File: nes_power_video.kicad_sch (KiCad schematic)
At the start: 13 parts, among them J2 Audio, J3 Video, J4 Conn_01x05, Q1 2SA1015

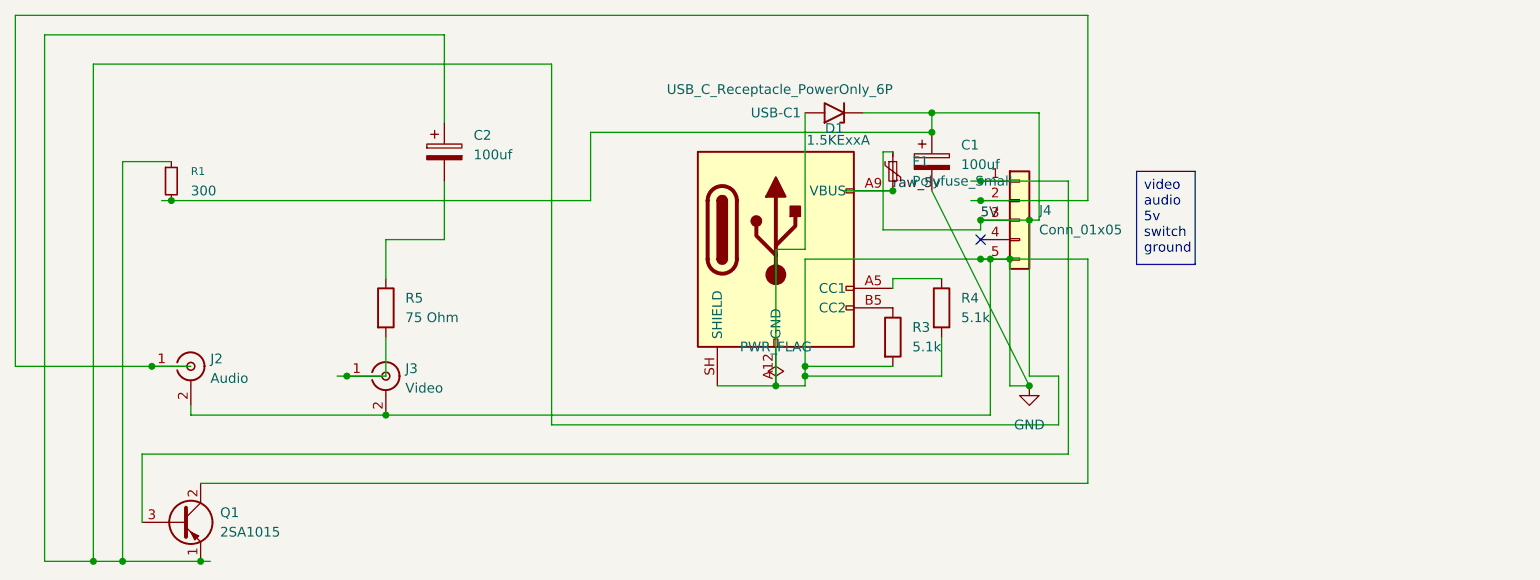
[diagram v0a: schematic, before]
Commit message: Switch J2/J3 to real PJRAN1X1U03X RCA jack symbols and re-route
J2 (Audio) and J3 (Video) were still using the generic
Connector:Conn_Coaxial symbol with the nes1:"nes connector" footprint.
Both now use the dedicated PJRAN1X1U03X symbol and matching footprint,
so the schematic and the board agree with the parts actually fitted.

PCB re-routed around the updated jacks: 47 -> 70 track segments, 6 -> 4
vias, footprint set unchanged.

Also stop tracking KiCad transient files (_autosave-*, *.lck) that were
committed by mistake, and add them to .gitignore.

Co-Authored-By: Claude Opus 5 <noreply@anthropic.com>
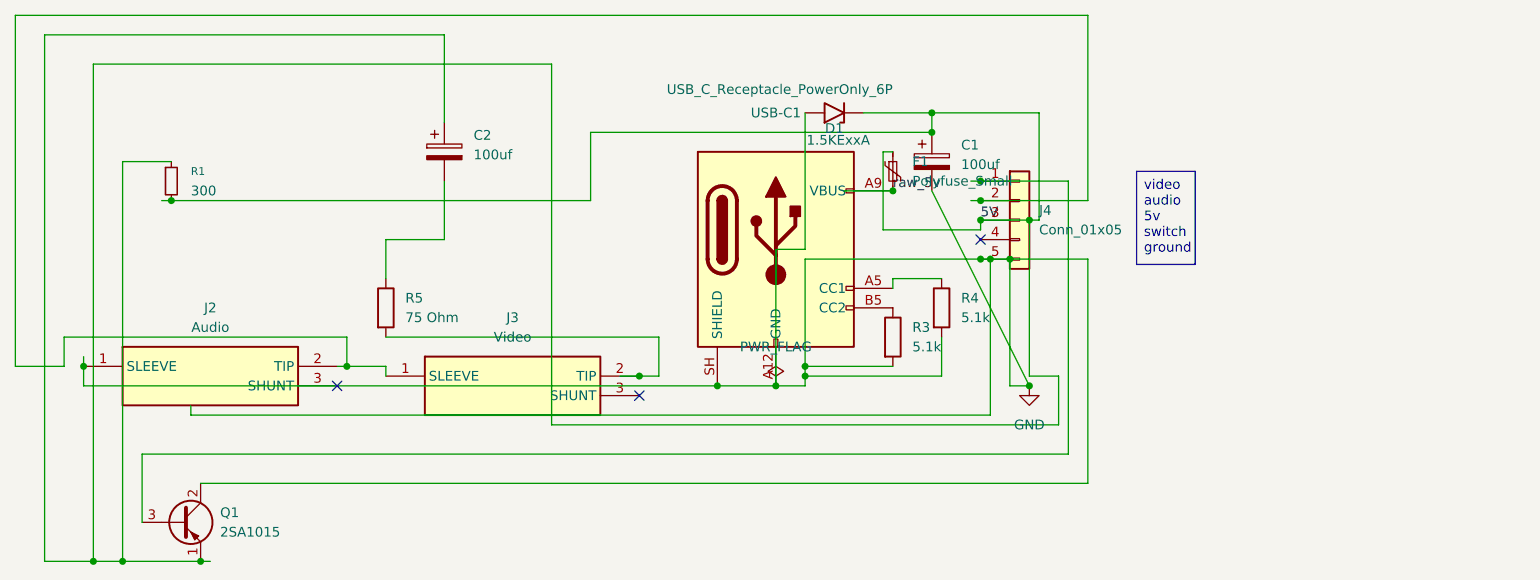
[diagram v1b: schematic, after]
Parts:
- J2, J3: footprint nes1:nes connector -> PJRAN1X1U03X; symbol Connector:Conn_Coaxial -> PJRAN1X1U03X:PJRAN1X1U03X; Height (none) -> 13; Manufacturer_Name (none) -> Switchcraft; Manufacturer_Part_Number (none) -> PJRAN1X1U03X; Mouser Part Number (none) -> 502-PJRAN1X1U03X; Mouser Price/Stock (none) -> https://www.mouser.co.uk/ProductDetail/Switchcraft/PJRAN1X1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
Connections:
- net GND: now also J2.1 (SLEEVE); no longer J2.2 (Ext), J3.2 (Ext)
- net at J4.2 (Pin_2): now also J2.2 (TIP), J3.1 (SLEEVE); no longer J2.1 (In)
- net at R5.2: now also J3.2 (TIP); no longer J3.1 (In)
- no-connect marks 1 -> 3

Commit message: Fix Q1 emitter node shorted to +5V rail (breaks video output)
R1 had both terminals on the /5V net, so Q1's emitter was clamped to the
rail and C2 coupled +5V rather than video into R5/J3. The composite
output could never have worked, on any v1 board.

Root cause: an R2 (110 ohm) sat between /5V and the emitter node until
2026-07-04. When it was deleted, KiCad merged its two leftover collinear
wire stubs into a single wire from (24.13,129.54) to (24.13,194.31),
welding the emitter node onto /5V and shorting R1 across it. Confirmed by
exporting netlists across the KiCad auto-backups: last good at 21:17:29,
broken at 22:15:13 the same evening.

Schematic: removed that wire plus the six-segment /5V run that existed
only to feed R2's top pin, and the junction dot left mid-wire. Netlist is
now /5V = C1.1 D1.1 F1.1 J4.3 R1.2 and Net-(Q1-E) = C2.1 Q1.1 R1.1, which
matches the last-good topology with R1 alone as the 300 ohm emitter load.
ERC is unchanged at 10 pre-existing warnings.

PCB: split the emitter node out of the /5V pour. Dropped the two traces
tying R1 pad 1 to the rail and the C2 branch that ran to R1 pad 2, moved
the C2 branch onto R1 pad 1, re-netted the Q1/C2 segments to Net-(Q1-E),
and routed R1 pad 2 to the rail down the clear corridor at x=47.5. Added
a short link restoring the F1 branch, which the deletions had otherwise
orphaned. DRC is identical to baseline: 2 pre-existing violations, 0
unconnected.

Chose R1 alone over restoring the R2 divider: in an emitter follower the
base sets the operating point, so the divider's shunt leg only burns
~6.5mA and drops the AC load from 100 to 52 ohms. R1 alone also matches
the BOM and needs no new footprint.

README documents the defect and the cut-and-verify rework for assembled
v1 boards.

Co-Authored-By: Claude Opus 5 <noreply@anthropic.com>
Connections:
- net 5V: no longer C2.1, Q1.1 (E), R1.1
- new net: C2.1, Q1.1 (E), R1.1
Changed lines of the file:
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@@
-	)
-	(junction
-		(at 24.13 194.31)
-		(diameter 0)
-		(color 0 0 0 0)
 	)
 	(junction
@@
 	(wire
 		(pts
-			(xy 24.13 129.54) (xy 83.82 129.54)
-		)
-		(stroke
-			(width 0)
-			(type default)
-		)
-	)
-	(wire
-		(pts
-			(xy 83.82 176.53) (xy 83.82 129.54)
-		)
-		(stroke
-			(width 0)
-			(type default)
-		)
-	)
-	(wire
-		(pts
 			(xy 30.48 189.23) (xy 30.48 180.34)
 		)
@@
 	(wire
 		(pts
-			(xy 24.13 129.54) (xy 24.13 194.31)
-		)
-		(stroke
-			(width 0)
-			(type default)
-		)
-	)
-	(wire
-		(pts
 			(xy 116.84 153.67) (xy 113.03 153.67)
 		)
@@
 	(wire
 		(pts
-			(xy 146.05 149.86) (xy 146.05 170.18)
-		)
-		(stroke
-			(width 0)
-			(type default)
-		)
-	)
-	(wire
-		(pts
 			(xy 27.94 194.31) (xy 38.1 194.31)
 		)
@@
 	(wire
 		(pts
-			(xy 149.86 170.18) (xy 149.86 176.53)
-		)
-		(stroke
-			(width 0)
-			(type default)
-		)
-	)
-	(wire
-		(pts
 			(xy 139.7 147.32) (xy 153.67 147.32)
 		)
@@
 	(wire
 		(pts
-			(xy 149.86 176.53) (xy 83.82 176.53)
-		)
-		(stroke
-			(width 0)
-			(type default)
-		)
-	)
-	(wire
-		(pts
 			(xy 62.23 165.1) (xy 97.79 165.1)
 		)
@@
 		)
 		(stroke
-			(width 0)
-			(type default)
-		)
-	)
-	(wire
-		(pts
-			(xy 146.05 170.18) (xy 149.86 170.18)
-		)
-		(stroke

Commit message: Add TPS2553 eFuse for real overcurrent protection
F1 (RHEF200, 2.0A hold / 3.8A trip) was the only overcurrent protection.
On a console drawing roughly 0.5-0.7A a 3.8A trip point protects nothing,
and a polyfuse takes seconds to act. U1 is now the real protection and F1
stays as a backup in case the eFuse fails short.

New power path:
  USB VBUS -> /raw_5v -> F1 -> /fused_5v -> U1 IN..OUT -> /5V -> load

U1 is a TI TPS2553DBVR adjustable current-limited switch in SOT-23-6:
resistor-programmed limit, ~3ms internal soft-start, thermal shutdown and
reverse-voltage protection. R6 = 22k sets a ~1.18A typical limit. Note the
relationship is inverse (I_OS ~ 25.9 / R_ILIM in kohm) - the datasheet spec
table gives 15k->1700mA, 20k->1295mA, 49.9k->520mA, 210k->130mA. C3 (100nF)
is U1's input decoupling, placed hard against pin 1 as TI requires.

EN is active-high on the TPS2553 and is tied to IN so the switch is always
on. FAULT is open-drain and left unconnected - nothing inside a closed NES
shell can read it. Ordered part is the plain TPS2553DBVR; the -1 suffix is
the latch-off variant, which would need a power cycle after each trip.

Pinout and the ILIM figures were taken from the TI datasheet rather than
from memory, which matters here: the pinout is IN/GND/EN/FAULT/ILIM/OUT
(pins 4 and 5 are easy to transpose) and an inverted reading of the ILIM
relationship would have produced a ~130mA limit that browns out the console.

Symbol: KiCad ships no TPS2553, so Custom.pretty/TPS2553DBV.kicad_sym adds
one, and a project sym-lib-table now registers it plus PJRAN1X1U03X so the
repo resolves its symbols without relying on a global table. Footprint is
the stock SOT-23-6_Handsoldering; R6/C3 are 0805 hand-solder.

PCB: U1, C3 and R6 sit in the band between R3 and D1 - the only pocket that
reaches F1's output, which the CC1/CC2 runs fence in on every other side.
The /5V spine is cut at (20.39,38.1)-(20.39,45) so F1 feeds U1's input, and
U1's output rejoins the spine. U1 is deliberat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
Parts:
- added C3: 100nF, Capacitor_SMD:C_0805_2012Metric_Pad1.18x1.45mm_HandSolder, symbol Device:C
- added R6: 22k, Resistor_SMD:R_0805_2012Metric_Pad1.20x1.40mm_HandSolder, symbol Device:R
- added U1: TPS2553DBV, Package_TO_SOT_SMD:SOT-23-6_Handsoldering, symbol TPS2553DBV:TPS2553DBV
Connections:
- net 5V: now also U1.6 (OUT); no longer F1.1
- net GND: now also C3.2, R6.2, U1.2 (GND)
- new net: R6.1, U1.5 (ILIM)
- new net fused_5v: C3.1, F1.1, U1.1 (IN), U1.3 (EN)
- no-connect marks 3 -> 4

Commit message: Fix J3 video jack sleeve wired to the audio net instead of GND
The PJRAN1X1U03X swap in 73425bb landed existing wires on different
pins: Conn_Coaxial and PJRAN1X1U03X number and place their pins
differently, so J3 pin 1 (SLEEVE) ended up on Net-(J2-TIP) instead of
GND. That left the video jack's shell with no ground return and tied
the audio signal to it.

Schematic: drop J3.1 off the audio net and run it to the GND bus at
y=171.45.

PCB: delete the three B.Cu segments spurring off J2.2 to J3.1, re-net
J3 pad 1 to GND, and refill the B.Cu ground zone. J3 pad 1 is a
plated through-hole, so the back-layer ground pour now connects it
directly -- no extra routing needed.

ERC unchanged (10 warnings, all pre-existing). DRC unchanged
(2 violations, all pre-existing) with 0 unconnected items, and all 16
nets cross-check pin-for-pin between schematic and PCB.

The fabbed v1 board is not affected: its IPC netlist has J3.2 on GND.

Co-Authored-By: Claude Opus 5 <noreply@anthropic.com>
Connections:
- net GND: now also J3.1 (SLEEVE)
- net at J2.2 (TIP), J4.2 (Pin_2): no longer J3.1 (SLEEVE)
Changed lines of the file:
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@@
 		)
+	)
+	(wire
+		(pts
+			(xy 62.23 170.18) (xy 62.23 171.45)
+		)
+		(stroke
+			(width 0)
+			(type default)
+		)
+	)
+	(junction
+		(at 62.23 171.45)
+		(diameter 0)
+		(color 0 0 0 0)
 	)
 	(junction
@@
 	(junction
 		(at 146.05 171.45)
-		(diameter 0)
-		(color 0 0 0 0)
-	)
-	(junction
-		(at 57.15 168.91)
 		(diameter 0)
 		(color 0 0 0 0)
@@
 	(wire
 		(pts
-			(xy 62.23 170.18) (xy 62.23 168.91)
-		)
-		(stroke
-			(width 0)
-			(type default)
-		)
-	)
-	(wire
-		(pts
 			(xy 116.84 168.91) (xy 128.27 168.91)
 		)
@@
 		)
 		(stroke
-			(width 0)
-			(type default)
-		)
-	)
-	(wire
-		(pts
-			(xy 57.15 168.91) (xy 62.23 168.91)
-		)
-		(stroke

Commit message: Add bring-up test points for video, GND, +5V and audio
Four through-hole test points (TestPoint_THTPad_D2.0mm_Drill1.0mm), one
per signal the v2 bring-up needs to see:

  TP1 /VIDEO_OUT  (62.0, 60.0)    F.Cu stub to the existing R5->J3 run
  TP2 GND         (58.5, 60.0)    straight into the B.Cu pour
  TP3 /5V         (52.0, 43.1)    sits on the protected 5 V trunk
  TP4 /AUDIO_OUT  (65.9, 28.35)   B.Cu stub to the J4.2 -> J2 run

Also names the two signal nets. They were auto-generated Net-(J3-TIP)
and Net-(J2-TIP); labelling them /VIDEO_OUT and /AUDIO_OUT is what lets
the test points attach by label instead of by geometry, and makes the
netlist readable.

Placement notes: TP3 and TP4 both started in the corridor between J2 and
J4 and could not clear each other's courtyards, so TP3 moved onto the
wide /5V trunk near Q1. TP4 sits in the 1.2 mm-wide window between the
J4-Pin_1 diagonal and the /5V diagonal; do not nudge it without
re-running DRC.

Verified: ERC 10 warnings / 0 errors and DRC 2 violations / 0 unconnected
items, both identical to the pre-change baseline. All 16 nets cross-check
pin-for-pin between schematic and PCB.

Co-Authored-By: Claude Opus 5 <noreply@anthropic.com>
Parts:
- added TP1: VIDEO, TestPoint:TestPoint_THTPad_D2.0mm_Drill1.0mm, symbol Connector:TestPoint
- added TP2: GND, TestPoint:TestPoint_THTPad_D2.0mm_Drill1.0mm, symbol Connector:TestPoint
- added TP3: +5V, TestPoint:TestPoint_THTPad_D2.0mm_Drill1.0mm, symbol Connector:TestPoint
- added TP4: AUDIO, TestPoint:TestPoint_THTPad_D2.0mm_Drill1.0mm, symbol Connector:TestPoint
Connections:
- net 5V: now also TP3.1
- net GND: now also TP2.1
- net AUDIO_OUT: now reaches J2.2 (TIP), J4.2 (Pin_2)
- net AUDIO_OUT: now also TP4.1
- net VIDEO_OUT: now reaches J3.2 (TIP), R5.2
- net VIDEO_OUT: now also TP1.1

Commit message: Add J5 feed header for the NESRGB 8-pin mini-DIN RGB connector
Provisions the Micomsoft XRGB-mini Framemeister connector standard that
the NESRGB board uses. The connector is NOT placed on this board: the
NESRGB kit ships it as a panel-mount jack that epoxies into a 12 mm hole
in the shell, so R/G/B run straight from the NESRGB to the connector and
this board only supplies the other three pins.

  J5.1 /RGB_VIDEO -> mini-DIN 3  composite video / sync, 75R
  J5.2 GND        -> mini-DIN 4
  J5.3 /5V        -> mini-DIN 5  (downstream of the TPS2553, so limited)

R7 (75 Ohm) is a second source termination off /VIDEO_BUF, mirroring R5.
Sharing R5 between the RCA jack and the mini-DIN would put two 75 Ohm
loads in parallel and halve the amplitude with both cables plugged in.

Also names the buffered video node: Net-(C2-Pad2) -> /VIDEO_BUF, so R7
can tap it by label.

Placement was constrained -- the Q1-E and VIDEO_BUF runs cut the lower
board in two on F.Cu, so J5's +5V leaves on B.Cu and vias up to R1.2.
J5 and R7 are placed from the libraries via pcbnew rather than embedded
by hand, which keeps them byte-identical to the library and avoids
lib_footprint_mismatch. The four test points also gained the
path/sheetname/sheetfile links they were missing, so a netlist re-import
will match them instead of duplicating them.

Caveat recorded in the README: two live outputs need R1 at 220 Ohm
rather than 330 Ohm, or the follower clips. Still unmeasured.

Verified: ERC 10 warnings / 0 errors and DRC 2 violations / 0 unconnected,
both identical to baseline. All 17 nets cross-check pin-for-pin.

Co-Authored-By: Claude Opus 5 <noreply@anthropic.com>
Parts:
- added J5: RGB conn feed, Connector_PinHeader_2.54mm:PinHeader_1x03_P2.54mm_Vertical, symbol Connector_Generic:Conn_01x03
- added R7: 75 Ohm, Resistor_THT:R_Axial_DIN0207_L6.3mm_D2.5mm_P7.62mm_Horizontal, symbol Device:R
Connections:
- net 5V: now also J5.3 (Pin_3)
- net GND: now also J5.2 (Pin_2)
- net VIDEO_BUF: now reaches C2.2, R5.1
- net VIDEO_BUF: now also R7.1
- new net RGB_VIDEO: J5.1 (Pin_1), R7.2
